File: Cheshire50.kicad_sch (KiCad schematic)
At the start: 132 parts, among them J1 JST_DB, J2 JST_PCB, SW1 MX_SW_HS, SW10 MX_SW_HS, SW11 MX_SW_HS, SW12 MX_SW_HS, SW13 MX_SW_HS, SW14 MX_SW_HS, SW15 MX_SW_HS, SW16 MX_SW_HS, SW17 MX_SW_HS, SW18 MX_SW_HS, SW19 MX_SW_HS, SW2 MX_SW_HS, SW20 MX_SW_HS, SW21 MX_SW_HS, SW22 MX_SW_HS, SW23 MX_SW_HS, SW24 MX_SW_HS, SW25 MX_SW_HS, SW26 MX_SW_HS, SW27 MX_SW_HS, SW28 MX_SW_HS, SW29 MX_SW_HS, SW3 MX_SW_HS, SW30 MX_SW_HS, SW31 MX_SW_HS, SW32 MX_SW_HS, SW33 MX_SW_HS, SW34 MX_SW_HS, SW35 MX_SW_HS, SW36 MX_SW_HS, SW37 MX_SW_HS, SW38 MX_SW_HS, SW39 MX_SW_HS, SW4 MX_SW_HS, SW40 MX_SW_HS, SW41 MX_SW_HS, SW42 MX_SW_HS, SW43 MX_SW_HS, SW44 MX_SW_HS, SW45 MX_SW_HS, SW46 MX_SW_HS, SW47 MX_SW_HS, SW48 MX_SW_HS, SW49 MX_SW_HS, SW5 MX_SW_HS, SW50 MX_SW_HS, SW51 MX_SW_HS, SW52 MX_SW_HS, SW53 MX_SW_HS, SW54 MX_SW_HS, SW55 MX_SW_HS, SW56 SW_Push, SW6 MX_SW_HS, SW7 MX_SW_HS, SW8 MX_SW_HS, SW9 MX_SW_HS, U1 ATMEGA32U4-AU, U2 PRTR5V0U2X, Y1 16MHz

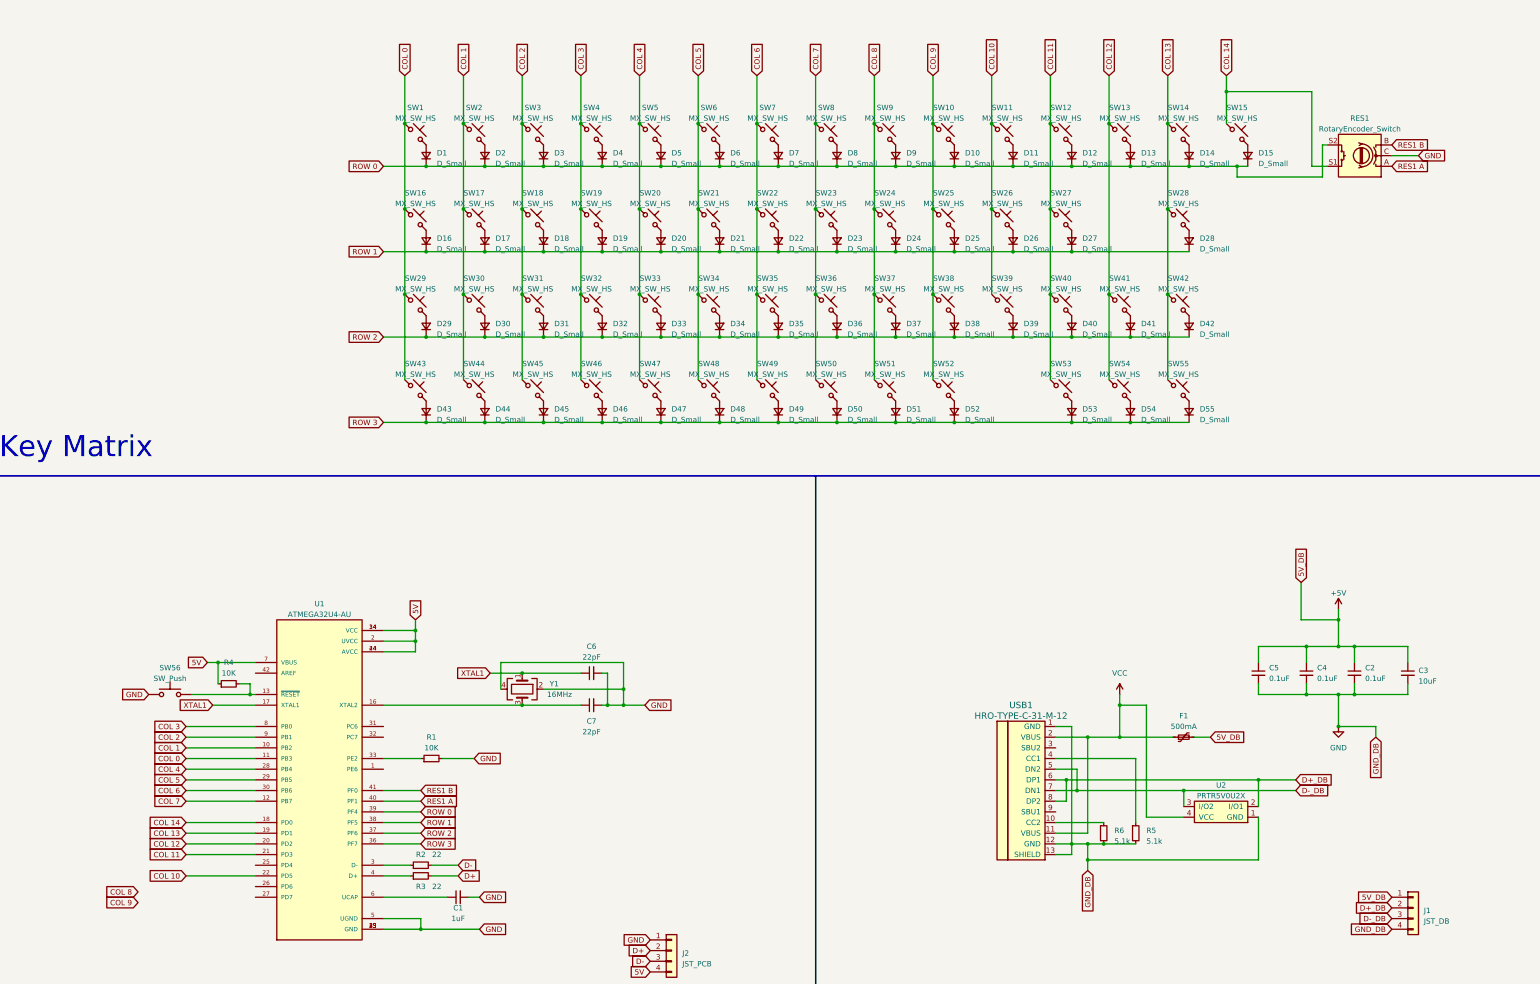
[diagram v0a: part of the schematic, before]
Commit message: new routing and logo
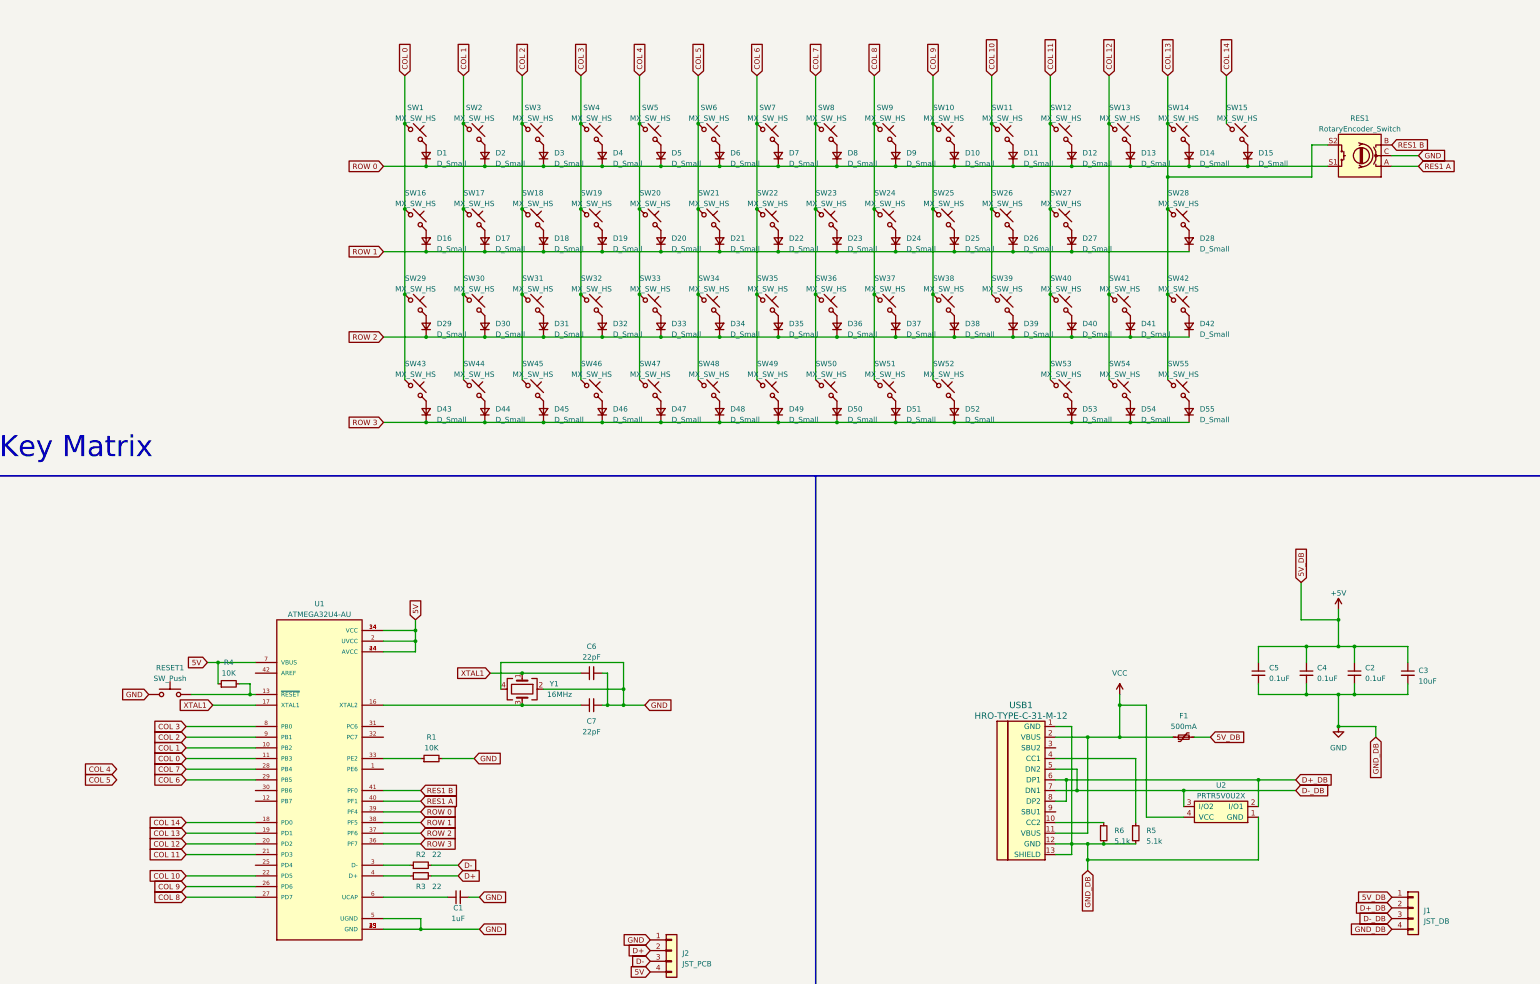
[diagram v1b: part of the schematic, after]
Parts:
- renumbered SW56 to RESET1
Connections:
- net COL 13: now also RES1.S2
- net COL 14: no longer RES1.S1
- net COL 4: no longer U1.28 (PB4)
- net COL 5: no longer U1.29 (PB5)
- net COL 6: now also U1.29 (PB5); no longer U1.30 (PB6)
- net COL 7: now also U1.28 (PB4); no longer U1.12 (PB7)
- net COL 8: now also U1.27 (PD7)
- net COL 9: now also U1.26 (PD6)
- net ROW 0: now also RES1.S1; no longer RES1.S2
